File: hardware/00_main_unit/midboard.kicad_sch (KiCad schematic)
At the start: 7 parts, among them J14 Conn_02x13_Odd_Even

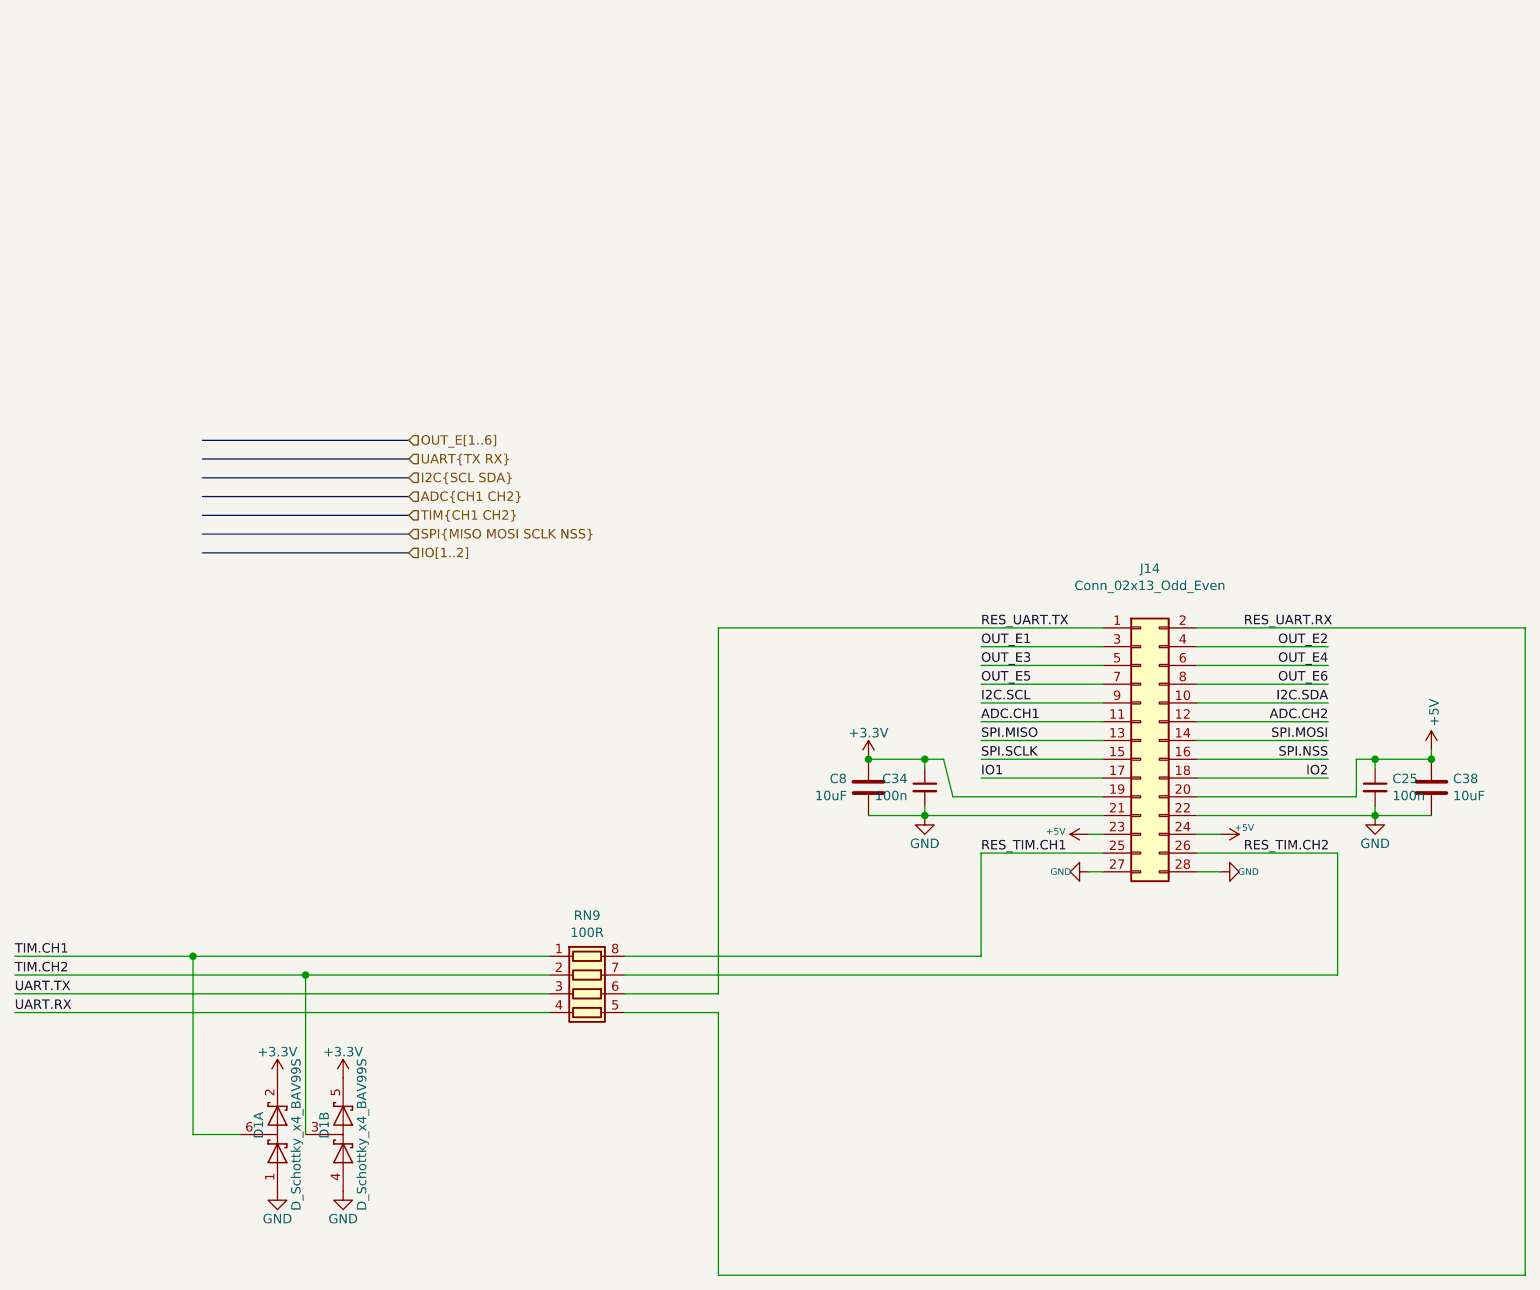
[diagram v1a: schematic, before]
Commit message: Remote mode fixes
Signed-off-by: Jarosław Karwik <jaroslaw.karwik@gmail.com>
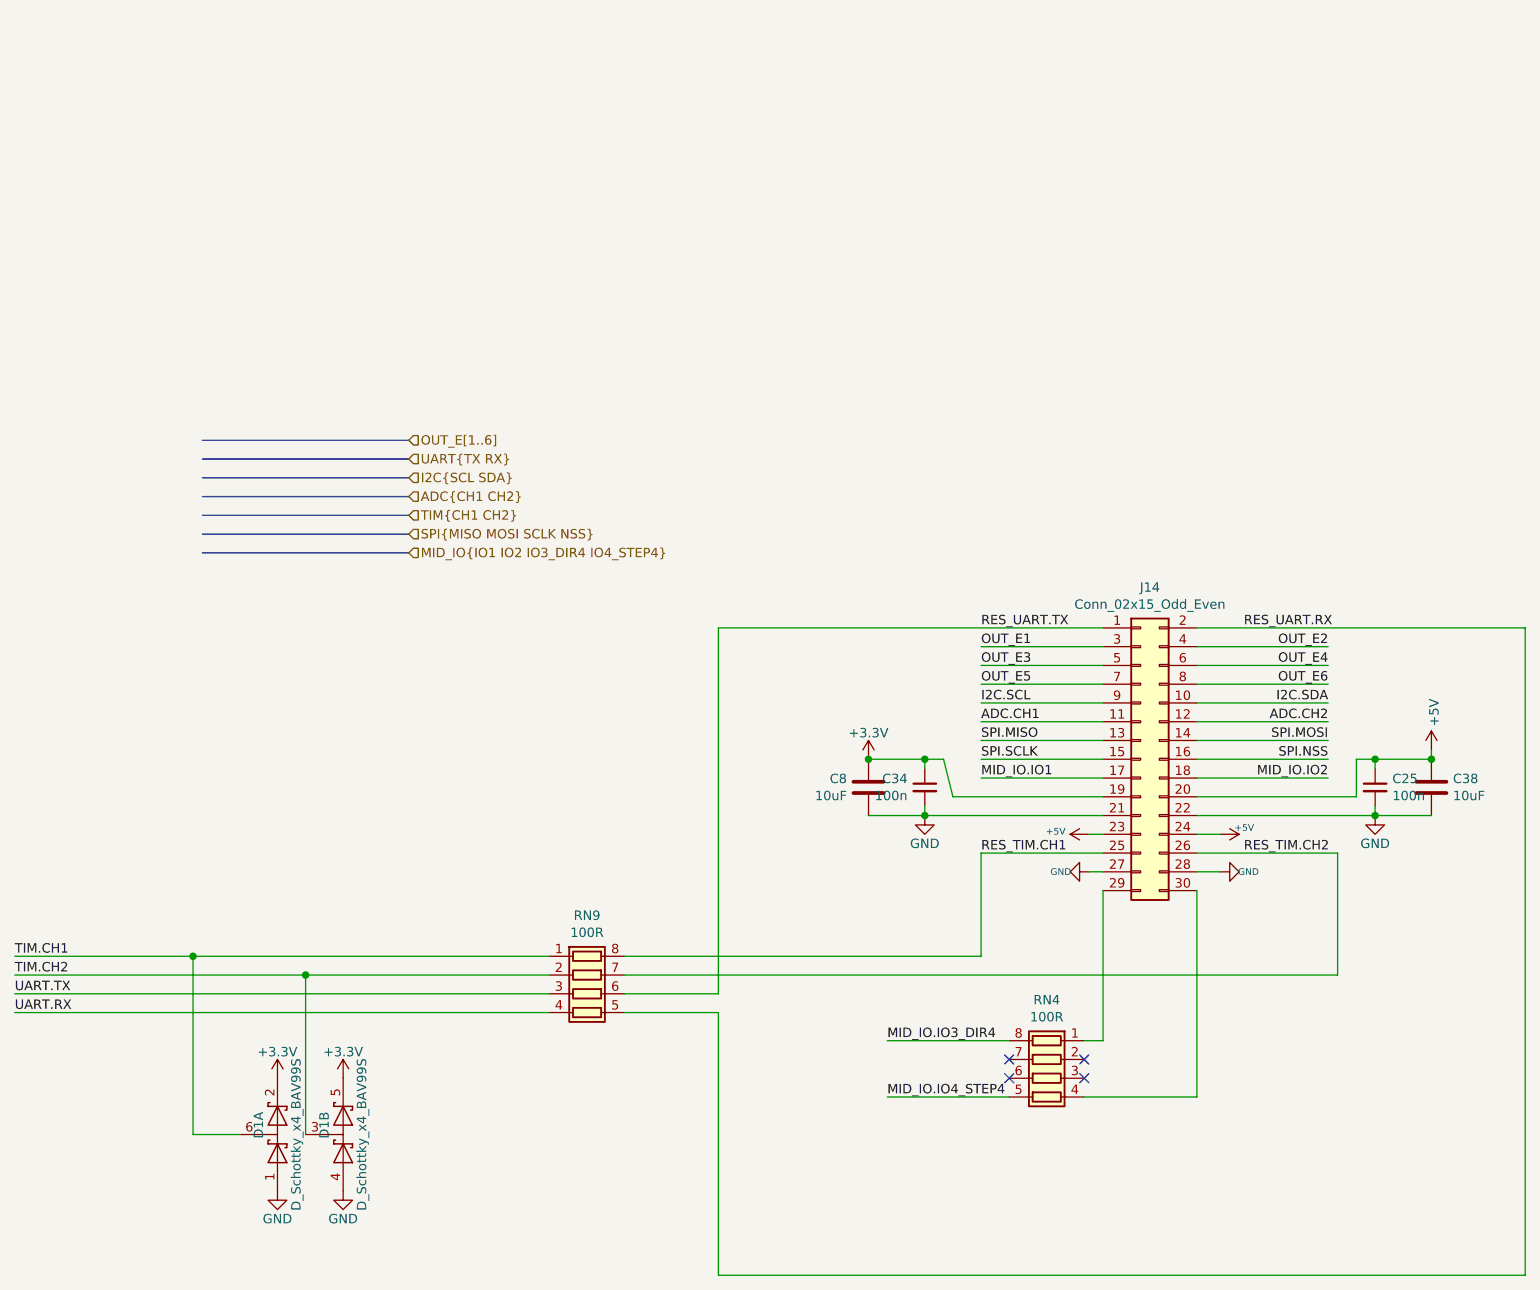
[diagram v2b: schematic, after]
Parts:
- added RN4: 100R, moje:R_Array_Convex_4x0603, symbol Uni_Printer-rescue:R_Pack04-Device
- J14: value Conn_02x13_Odd_Even -> Conn_02x15_Odd_Even; footprint Connector_PinHeader_2.54mm:PinHeader_2x14_P2.54mm_Vertical -> Connector_PinHeader_2.54mm:PinHeader_2x15_P2.54mm_Vertical; symbol Connector_Generic:Conn_02x14_Odd_Even -> Connector_Generic:Conn_02x15_Odd_Even
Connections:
- net IO1 renamed MID_IO.IO1
- net IO2 renamed MID_IO.IO2
- new net: J14.29 (Pin_29), RN4.1 (R1.1)
- new net: J14.30 (Pin_30), RN4.4 (R4.1)
- new net MID_IO.IO3_DIR4: RN4.8 (R1.2)
- new net MID_IO.IO4_STEP4: RN4.5 (R4.2)
- no-connect marks 0 -> 4

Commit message: FW and SW updates for new revision
Signed-off-by: Jarosław Karwik <jaroslaw.karwik@gmail.com>
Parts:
- removed C25, C34: 100n, Capacitor_SMD:C_0603_1608Metric, symbol Uni_Printer-rescue:C_Small-Device
- removed C38, C8: 10uF, Capacitor_SMD:C_0603_1608Metric, symbol Uni_Printer-rescue:C-Device
- removed D1: D_Schottky_x4_BAV99S, moje:SOT-363, symbol Uni_Printer-rescue:D_Schottky_x4_BAV99S-RESCUE-step2cnc-Sensor_tank_v1-rescue-U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
- removed J14: Conn_02x15_Odd_Even, Connector_PinHeader_2.54mm:PinHeader_2x15_P2.54mm_Vertical, symbol Connector_Generic:Conn_02x15_Odd_Even
- removed RN4, RN9: 100R, moje:R_Array_Convex_4x0603, symbol Uni_Printer-rescue:R_Pack04-Device
- added J?: Conn_02x15_Odd_Even, Connector_PinHeader_2.54mm:PinHeader_2x07_P2.54mm_Vertical, symbol Connector_Generic:Conn_02x07_Odd_Even
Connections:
- net +3V3: now also J?.11 (Pin_11)
- net +5V: now also J?.9 (Pin_9)
- net ADC.CH1: now also J?.13 (Pin_13)
- net ADC.CH2: now also J?.14 (Pin_14)
- net GND: now also J?.10 (Pin_10), J?.12 (Pin_12)
- net I2C.SCL: now also J?.7 (Pin_7)
- net I2C.SDA: now also J?.8 (Pin_8)
- net OUT_E1: now also J?.1 (Pin_1)
- net OUT_E2: now also J?.2 (Pin_2)
- net OUT_E3: now also J?.3 (Pin_3)
- net OUT_E4: now also J?.4 (Pin_4)
- net OUT_E5: now also J?.5 (Pin_5)
- net OUT_E6: now also J?.6 (Pin_6)
- no-connect marks 4 -> 0
